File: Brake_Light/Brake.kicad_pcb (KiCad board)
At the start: 2 copper layers, 64 x 64 mm, 72 parts, among them J1 Conn_01x03, J10 Conn_01x08, J11 Conn_01x08, J13 Conn_01x08, J14 Conn_01x08, J15 Conn_01x08, J16 Conn_01x08, J17 Conn_01x08, J3 Conn_01x05, J4 Conn_01x05, J9 Conn_01x08, SW1 SW_SPST, SW2 SW_SPST, U1 STM32F103C8Tx, U2 SN65HVD256D, U4 AP2204K-ADJ, U5 AP63200WU, U6 MAX7219CNG, U7 MAX7219CNG, U8 MAX7219CNG, U9 MAX7219CNG, Y1 8M, Y2 32.768k

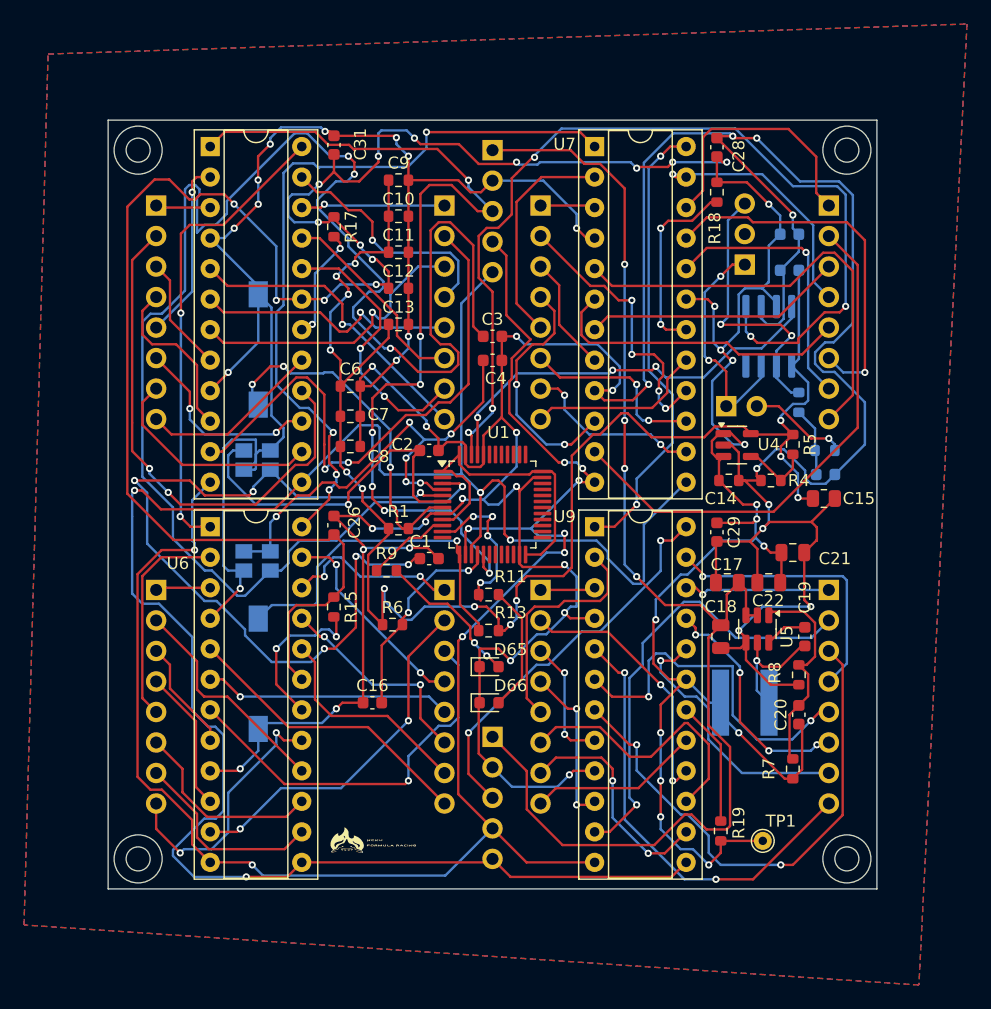
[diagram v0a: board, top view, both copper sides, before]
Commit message: fix: mounting hole
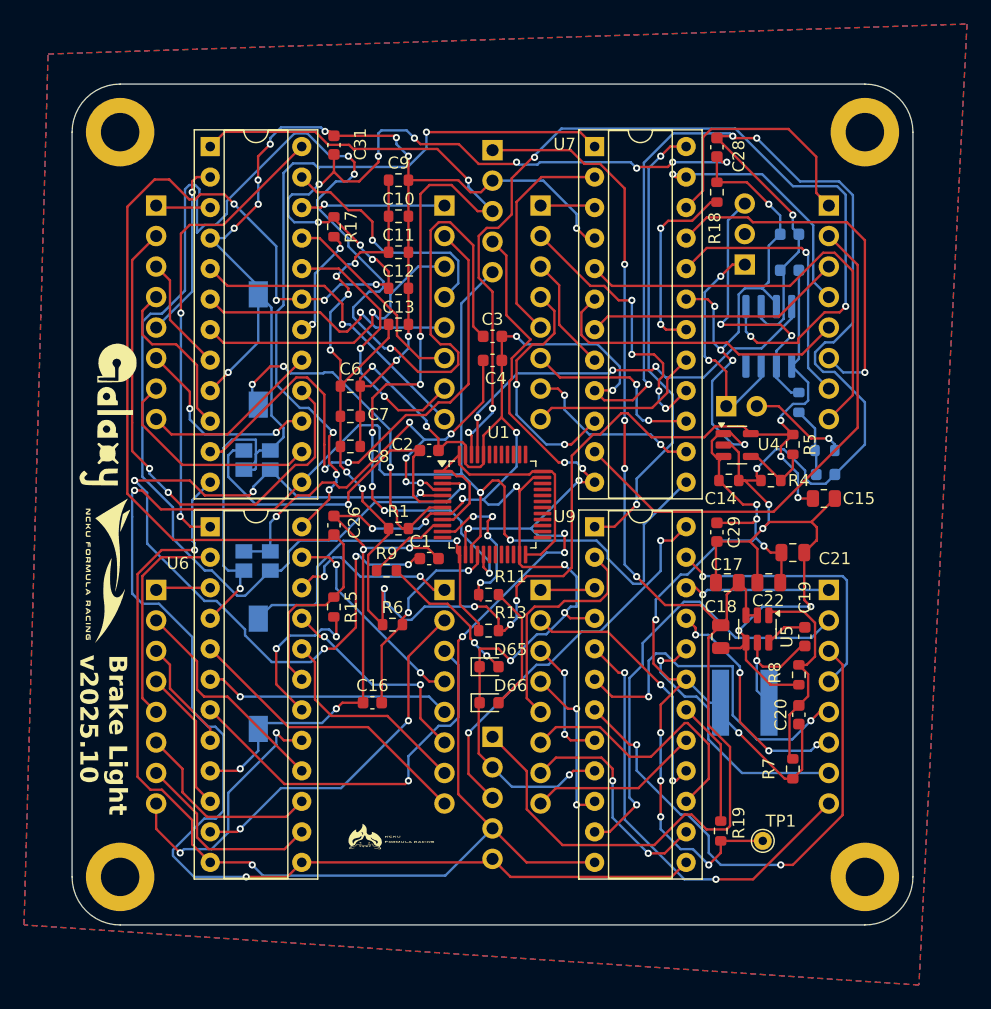
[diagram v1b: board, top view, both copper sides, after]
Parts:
- added G***: LOGO, LOGO, F.Cu at (160.0, 97.5)
- added G***: LOGO, LOGO, F.Cu at (160.0, 84.5)
- added H1: MountingHole_Pad, MountingHole:MountingHole_3.2mm_M3_ISO7380_Pad, F.Cu at (161.0, 61.0)
- added H2: MountingHole_Pad, MountingHole:MountingHole_3.2mm_M3_ISO7380_Pad, F.Cu at (223.0, 61.0)
- added H3: MountingHole_Pad, MountingHole:MountingHole_3.2mm_M3_ISO7380_Pad, F.Cu at (223.0, 123.0)
- added H4: MountingHole_Pad, MountingHole:MountingHole_3.2mm_M3_ISO7380_Pad, F.Cu at (161.0, 123.0)
- moved G*** 1.53 mm to (183.5, 119.5)
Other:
- board size 64 x 64 mm -> 70 x 70 mm
- board text added: "Brake Light v2025.10"
